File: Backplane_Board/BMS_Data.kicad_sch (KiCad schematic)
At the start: 8 parts, among them J22 Conn_01x07_Female, U5 PINA740AIREMR

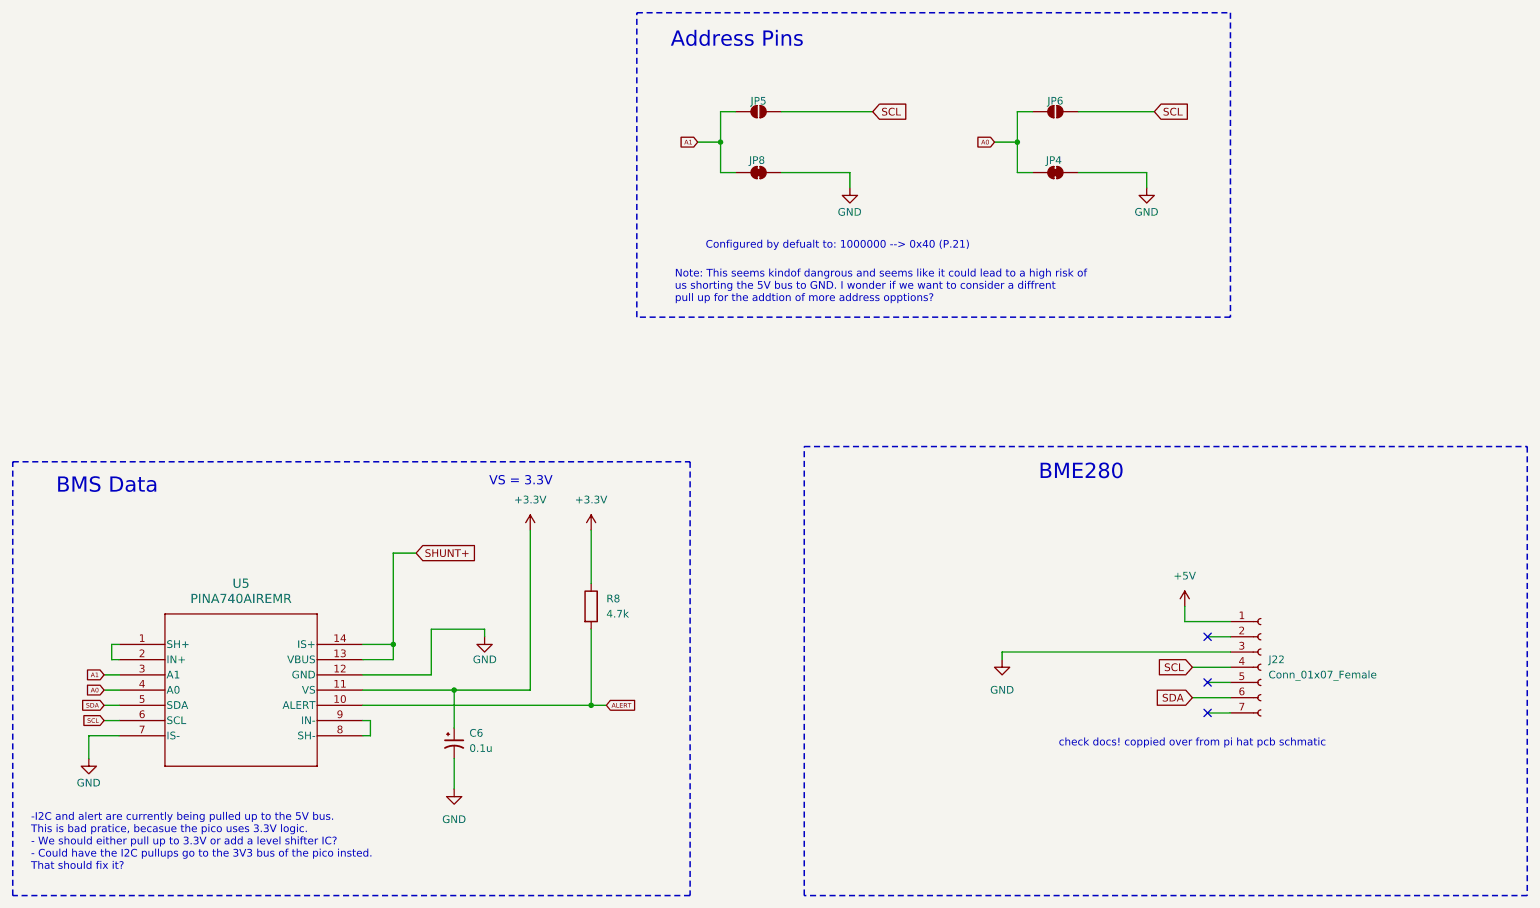
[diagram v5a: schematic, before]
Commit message: update FET circits
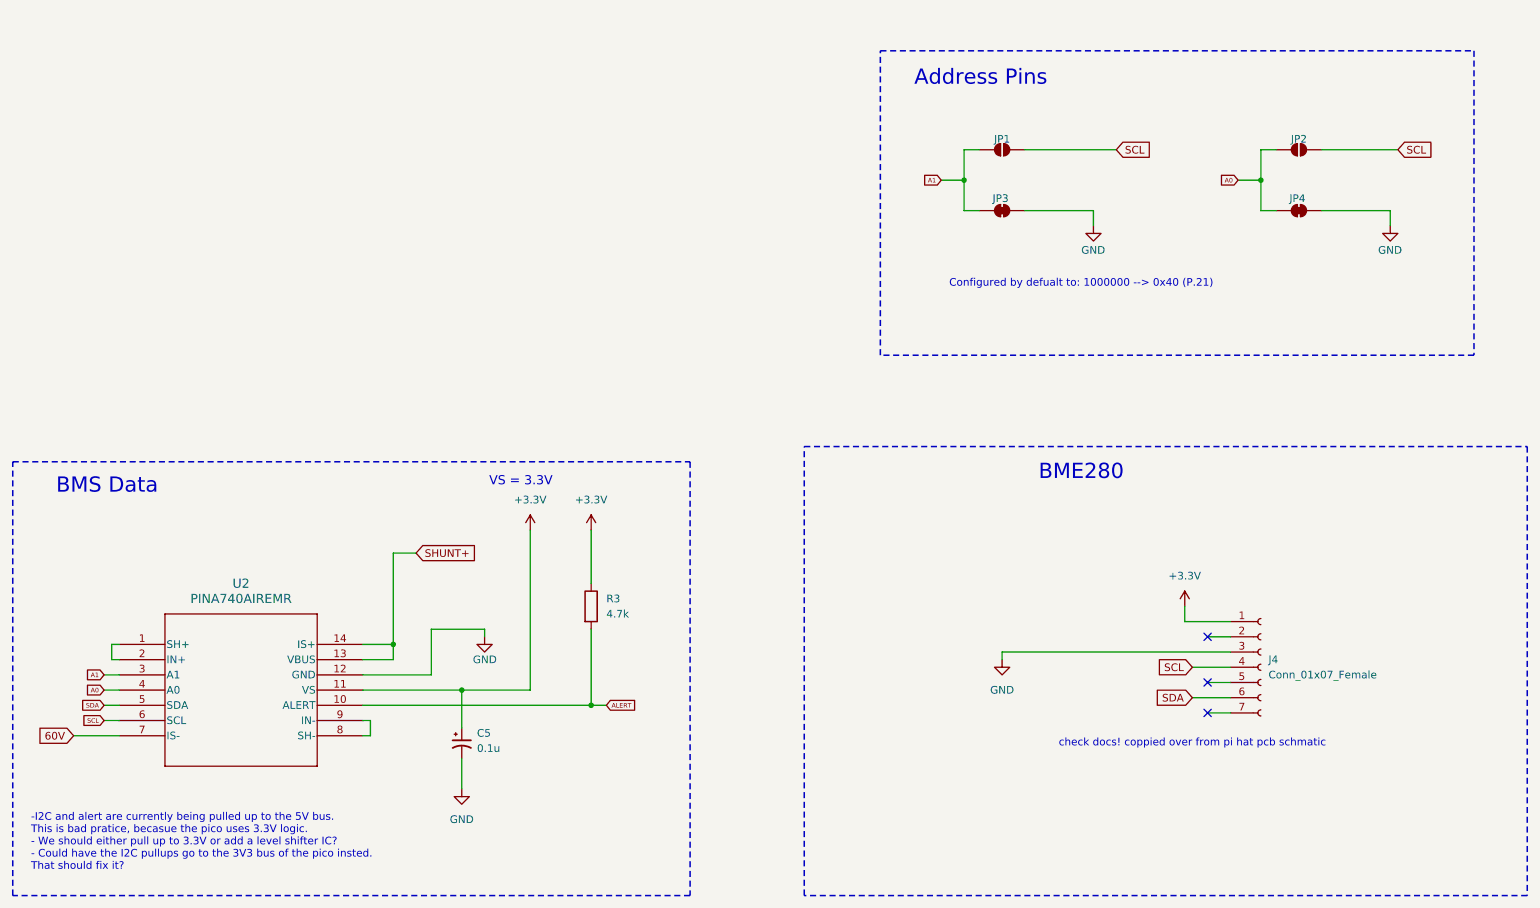
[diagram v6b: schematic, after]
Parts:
- JP1: renamed from JP5; footprint (none) -> Jumper:SolderJumper-2_P1.3mm_Open_RoundedPad1.0x1.5mm
- JP2: renamed from JP6; footprint (none) -> Jumper:SolderJumper-2_P1.3mm_Open_RoundedPad1.0x1.5mm
- JP3: renamed from JP8; footprint (none) -> Jumper:SolderJumper-2_P1.3mm_Bridged_RoundedPad1.0x1.5mm
- JP4: footprint (none) -> Jumper:SolderJumper-2_P1.3mm_Bridged_RoundedPad1.0x1.5mm
- renumbered C6 to C5, J22 to J4, R8 to R3, U5 to U2
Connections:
- net +5V is gone; now on net +3.3V: J4.1 (Pin_1)
- net GND: no longer U2.7 (IS-)
- new net 60V: U2.7 (IS-)
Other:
- note removed: "Note: This seems kindof dangrous and seems like it could lead to a high risk of us shorting the 5V bus to GND. I wonder if we want to consider a diffrent pull up for the addtion of more address opptions?"
- moved on the sheet: C5, JP1, JP2, JP3, JP4

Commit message: adding more footprints
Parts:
- C5: footprint (none) -> Capacitor_SMD:C_0603_1608Metric_Pad1.08x0.95mm_HandSolder
- R3: footprint (none) -> Resistor_SMD:R_1206_3216Metric_Pad1.30x1.75mm_HandSolder
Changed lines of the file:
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@@
 			)
 		)
-		(property "Footprint" ""
+		(property "Footprint" "Resistor_SMD:R_1206_3216Metric_Pad1.30x1.75mm_HandSolder"
 			(at 116.332 116.84 90)
 			(effects
@@
 			)
 		)
-		(property "Footprint" ""
+		(property "Footprint" "Capacitor_SMD:C_0603_1608Metric_Pad1.08x0.95mm_HandSolder"
 			(at 96.52 139.7 0)
 			(effects

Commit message: derat nest ifcation
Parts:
- R3: footprint Resistor_SMD:R_1206_3216Metric_Pad1.30x1.75mm_HandSolder -> Resistor_SMD:R_0805_2012Metric_Pad1.20x1.40mm_HandSolder
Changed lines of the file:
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@@
 			)
 		)
-		(property "Footprint" "Resistor_SMD:R_1206_3216Metric_Pad1.30x1.75mm_HandSolder"
+		(property "Footprint" "Resistor_SMD:R_0805_2012Metric_Pad1.20x1.40mm_HandSolder"
 			(at 116.332 116.84 90)
 			(effects
